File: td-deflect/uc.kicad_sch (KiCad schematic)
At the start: 20 parts, among them J4 Conn_ARM_JTAG_SWD_10, J6 Conn_01x06_Male, U12 LM1117-5.0, U2 STM32G474RETx, U23 TPS70933, U3 INA193, U4 TPS70933, X1 SG-8002CA

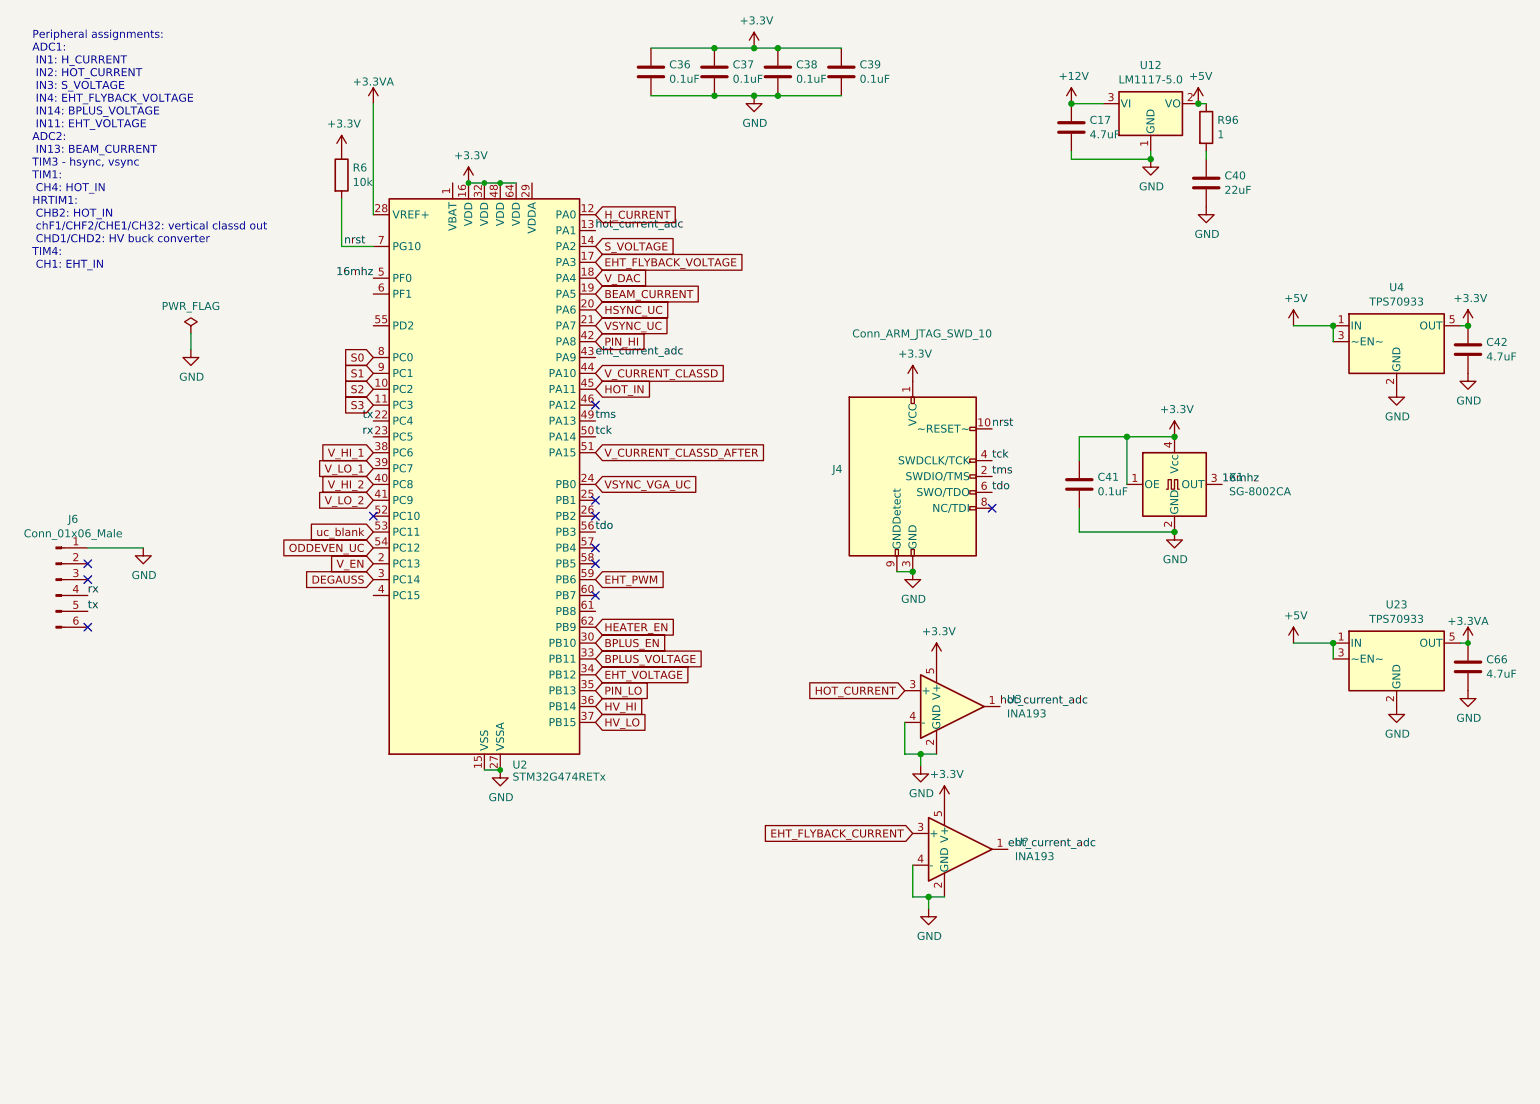
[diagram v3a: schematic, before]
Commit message: modify flyback feedback mechanism
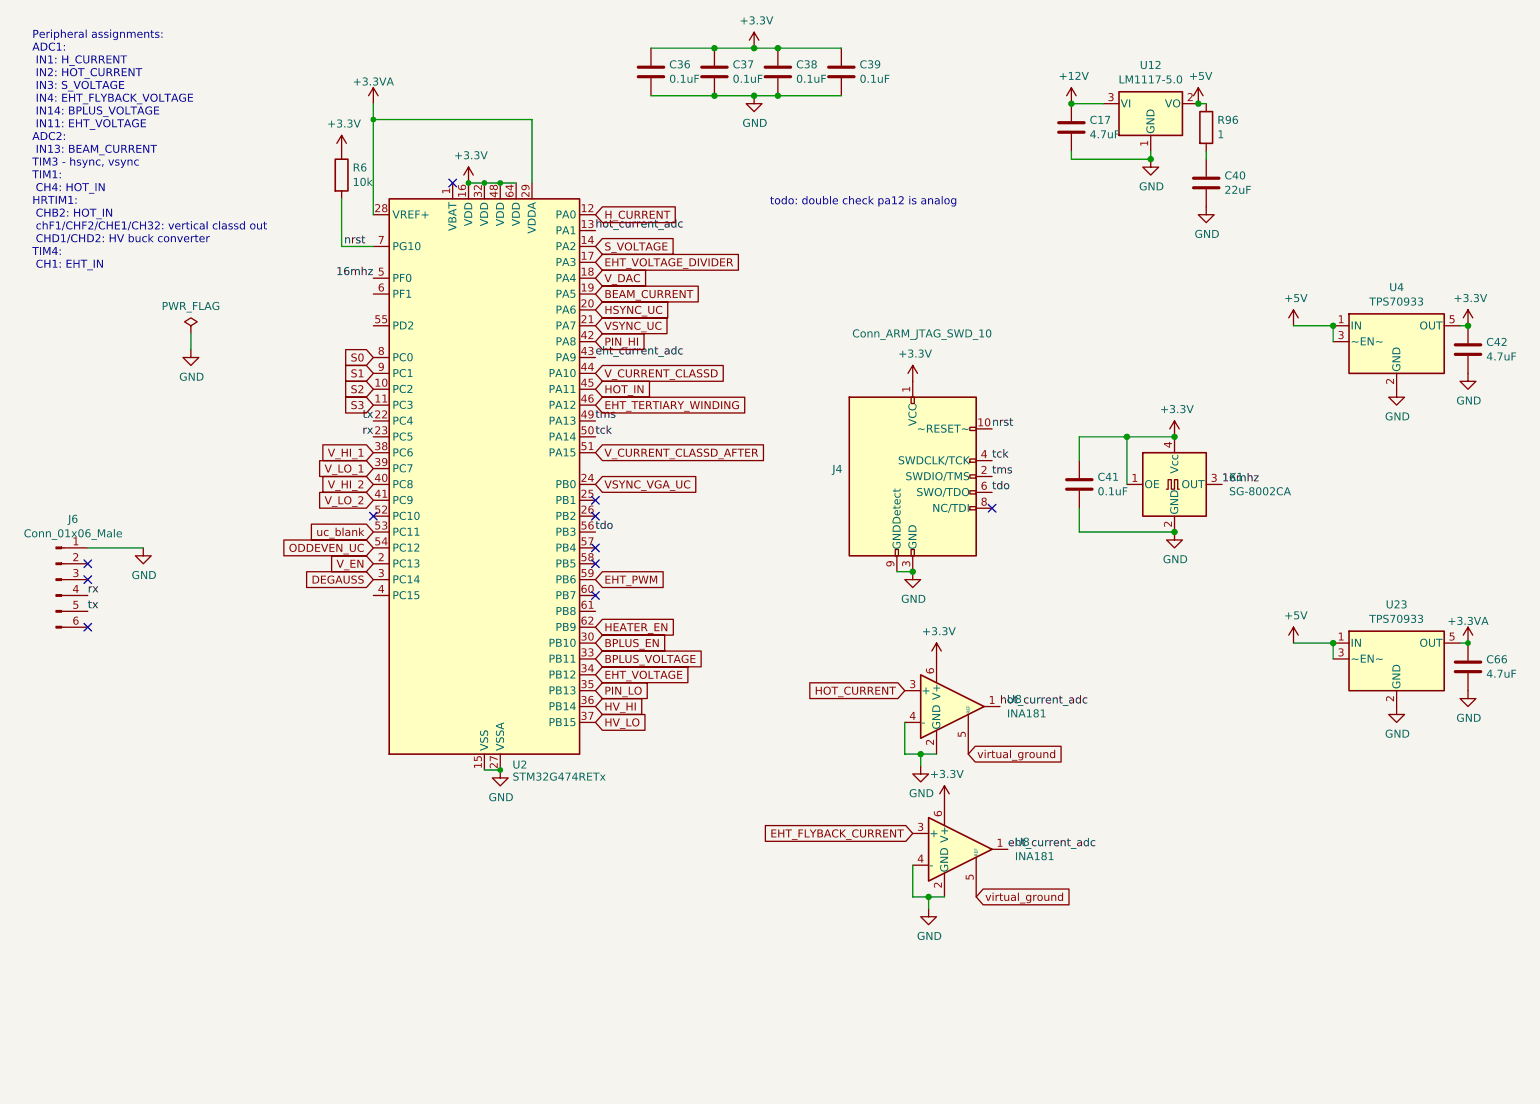
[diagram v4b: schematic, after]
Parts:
- removed U3, U?: INA193, Package_TO_SOT_SMD:SOT-23-5, symbol Amplifier_Current:INA193
- added U8 (x2): INA181, Package_TO_SOT_SMD:SOT-23-6, symbol Amplifier_Current:INA181
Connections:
- net +3.3VA: now also U2.29 (VDDA)
- net +3V3: now also U8.6 (V+), U8.6 (V+)
- net EHT_FLYBACK_CURRENT: now also U8.3 (+)
- net GND: now also U8.2 (GND), U8.2 (GND), U8.4 (-), U8.4 (-)
- net HOT_CURRENT: now also U8.3 (+)
- net eht_current_adc: now also U8.1
- net hot_current_adc: now also U8.1
- net EHT_TERTIARY_WINDING: now reaches U2.46 (PA12)
- net EHT_FLYBACK_VOLTAGE renamed EHT_VOLTAGE_DIVIDER
- new net virtual_ground: U8.5 (REF), U8.5 (REF)
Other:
- note added: "todo: double check pa12 is analog"
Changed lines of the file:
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@@
   (junction (at 224.79 83.82) (diameter 1.016) (color 0 0 0 0)
+  )
+  (junction (at 96.52 33.02) (diameter 0) (color 0 0 0 0)
   )
   (junction (at 151.13 29.21) (diameter 1.016) (color 0 0 0 0)
@@
   (no_connect (at 132.08 101.6))
   (no_connect (at 50.8 104.14))
+  (no_connect (at 109.22 43.18))
   (no_connect (at 132.08 96.52))
   (no_connect (at 50.8 114.3))
@@
   (no_connect (at 96.52 96.52))
   (no_connect (at 132.08 104.14))
-  (no_connect (at 132.08 78.74))
   (no_connect (at 132.08 93.98))
   (wire (pts (xy 208.28 39.37) (xy 220.98 39.37))
@@
     (stroke (width 0) (type solid))
   )
+  (wire (pts (xy 121.92 33.02) (xy 121.92 43.18))
+    (stroke (width 0) (type default))
+  )
   (wire (pts (xy 209.55 83.82) (xy 217.17 83.82))
     (stroke (width 0) (type solid))
@@
     (stroke (width 0) (type solid))
   )
+  (wire (pts (xy 96.52 33.02) (xy 96.52 48.26))
+    (stroke (width 0) (type default))
+  )
   (wire (pts (xy 91.44 53.34) (xy 91.44 45.72))
     (stroke (width 0) (type default))
@@
     (stroke (width 0) (type solid))
   )
+  (wire (pts (xy 96.52 33.02) (xy 121.92 33.02))
+    (stroke (width 0) (type default))
+  )
   (wire (pts (xy 182.88 157.48) (xy 185.42 157.48))
     (stroke (width 0) (type solid))
@@
     (stroke (width 0) (type default))
   )
-  (wire (pts (xy 96.52 30.48) (xy 96.52 48.26))
+  (wire (pts (xy 96.52 30.48) (xy 96.52 33.02))
     (stroke (width 0) (type default))
   )
@@
     (effects (font (size 1.27 1.27)) (justify left bottom))
   )
+  (text "todo: double check pa12 is analog" (at 160.02 46.99 0)
+    (effects (font (size 1.27 1.27)) (justify left bottom))
+  )
   (label "tx" (at 50.8 111.76 0) (fields_autoplaced)
     (effects (font (size 1.27 1.27)) (justify left bottom))
@@
   (label "rx" (at 96.52 83.82 180) (fields_autoplaced)
     (effects (font (size 1.27 1.27)) (justify right bottom))
-  )
-  (global_label "EHT_FLYBACK_VOLTAGE" (shape input) (at 132.08 55.88 0) (fields_autoplaced)
-    (effects (font (size 1.27 1.27)) (justify left))
-    (property "Intersheetrefs" "${INTERSHEET_REFS}" (at 155.7402 55.88 0)
-      (effects (font (size 1.27 1.27)) (justify left) hide)
-    )
   )
   (global_label "S0" (shape input) (at 96.52 71.12 180) (fields_autoplaced)
@@
     )
   )
+  (global_label "virtual_ground" (shape input) (at 193.04 157.48 0) (fields_autoplaced)
+    (effects (font (size 1.27 1.27)) (justify left))
+    (property "Intersheetrefs" "${INTERSHEET_REFS}" (at 208.8379 157.48 0)
+      (effects (font (size 1.27 1.27)) (justify left) hide)
+    )
+  )
   (global_label "HOT_IN" (shape input) (at 132.08 76.2 0) (fields_autoplaced)
     (effects (font (size 1.27 1.27)) (justify left))
@@
     )
   )
+  (global_label "virtual_ground" (shape input) (at 191.77 134.62 0) (fields_autoplaced)
+    (effects (font (size 1.27 1.27)) (justify left))
+    (property "Intersheetrefs" "${INTERSHEET_REFS}" (at 207.5679 134.62 0)
+      (effects (font (size 1.27 1.27)) (justify left) hide)
+    )
+  )
   (global_label "VSYNC_VGA_UC" (shape input) (at 132.08 91.44 0) (fields_autoplaced)
     (effects (font (size 1.27 1.27)) (justify left))
@@
     )
   )
+  (global_label "EHT_VOLTAGE_DIVIDER" (shape input) (at 132.08 55.88 0) (fields_autoplaced)
+    (effects (font (size 1.27 1.27)) (justify left))
+    (property "Intersheetrefs" "${INTERSHEET_REFS}" (at 154.8935 55.88 0)
+      (effects (font (size 1.27 1.27)) (justify left) hide)
+    )
+  )
   (global_label "BPLUS_VOLTAGE" (shape input) (at 132.08 119.38 0) (fields_autoplaced)
     (effects (font (size 1.27 1.27)) (justify left))
@@
     )
   )
+  (global_label "EHT_TERTIARY_WINDING" (shape input) (at 132.08 78.74 0) (fields_autoplaced)
+    (effects (font (size 1.27 1.27)) (justify left))
+    (property "Intersheetrefs" "${INTERSHEET_REFS}" (at 155.9821 78.74 0)
+      (effects (font (size 1.27 1.27)) (justify left) hide)
+    )
+  )
   (global_label "S3" (shape input) (at 96.52 78.74 180) (fields_autoplaced)
     (effects (font (size 1.27 1.27)) (justify right))
@@
         (path "/55a1a5e1-4d11-4c3e-b2b4-b9d50ddc5f9d/00000000-0000-0000-0000-00005c37bef7"
           (reference "#PWR0140") (unit 1)
-        )
-      )
-    )
-  )
-  (symbol (lib_id "Amplifier_Current:INA193") (at 189.23 127 0) (unit 1)
-    (in_bom yes) (on_board yes) (dnp no)
-    (property "Reference" "U3" (at 197.9676 125.8316 0)
-      (effects (font (size 1.27 1.27)) (justify left))
-    )
-    (property "Value" "INA193" (at 197.9676 128.143 0)
-      (effects (font (size 1.27 1.27)) (justify left))
-    )
-    (property "Footprint" "Package_TO_SOT_SMD:SOT-23-5" (at 189.23 127 0)
-      (effects (font (size 1.27 1.27)) hide)
-    )
-    (property "Datasheet" "http://www.ti.com/lit/ds/symlink/ina193.pdf" (at 189.23 127 0)
-      (effects (font (size 1.27 1.27)) hide)
-    )
-    (property "Digikey" "296-26065-1-ND" (at 189.23 127 0)
-      (effects (font (size 1.27 1.27)) hide)
-    )
-    (pin "1")
-    (pin "2")
-    (pin "3")
-    (pin "4")
-    (pin "5")
-    (instances
-      (project "td-deflect"
-        (path "/55a1a5e1-4d11-4c3e-b2b4-b9d50ddc5f9d/00000000-0000-0000-0000-00005c37bef7"
-          (reference "U3") (unit 1)
         )
       )
@@
     )
   )
-  (symbol (lib_id "Amplifier_Current:INA193") (at 190.5 149.86 0) (unit 1)
-    (in_bom yes) (on_board yes) (dnp no)
-    (property "Reference" "U?" (at 199.2376 148.6916 0)
-      (effects (font (size 1.27 1.27)) (justify left))
-    )
-    (property "Value" "INA193" (at 199.2376 151.003 0)
-      (effects (font (size 1.27 1.27)) (justify left))
-    )
-    (property "Footprint" "Package_TO_SOT_SMD:SOT-23-5" (at 190.5 149.86 0)
-      (effects (font (size 1.27 1.27)) hide)
-    )
-    (property "Datasheet" "http://www.ti.com/lit/ds/symlink/ina193.pdf" (at 190.5 149.86 0)
-      (effects (font (size 1.27 1.27)) hide)
-    )
-    (property "Digikey" "296-26065-1-ND" (at 190.5 149.86 0)
+  (symbol (lib_id "Amplifier_Current:INA181") (at 189.23 127 0) (unit 1)
+    (in_bom yes) (on_board yes) (dnp no)
+    (property "Reference" "U8" (at 197.9676 125.8316 0)
+      (effects (font (size 1.27 1.27)) (justify left))
+    )
+    (property "Value" "INA181" (at 197.9676 128.143 0)
+      (effects (font (size 1.27 1.27)) (justify left))
+    )
+    (property "Footprint" "Package_TO_SOT_SMD:SOT-23-6" (at 190.5 125.73 0)
+      (effects (font (size 1.27 1.27)) hide)
+    )
+    (property "Datasheet" "http://www.ti.com/lit/ds/symlink/ina181.pdf" (at 193.04 123.19 0)
+      (effects (font (size 1.27 1.27)) hide)
+    )
+    (property "Digikey" "296-47658-1-ND" (at 189.23 127 0)
       (effects (font (size 1.27 1.27)) hide)
     )
@@
     (pin "4")
     (pin "5")
-    (instances
-      (project "td-deflect"
-        (path "/55a1a5e1-4d11-4c3e-b2b4-b9d50ddc5f9d/00000000-0000-0000-0000-00005c37bef7"
-          (reference "U?") (unit 1)
+    (pin "6")
+    (instances
+      (project "td-deflect"
+        (path "/55a1a5e1-4d11-4c3e-b2b4-b9d50ddc5f9d"
+          (reference "U8") (unit 1)
+        )
+        (path "/55a1a5e1-4d11-4c3e-b2b4-b9d50ddc5f9d/00000000-0000-0000-0000-00005c37bef7"
+          (reference "U3") (unit 1)
         )
       )
@@
         )
       )
+    )
+  )
+  (symbol (lib_id "Amplifier_Current:INA181") (at 190.5 149.86 0) (unit 1)
+    (in_bom yes) (on_board yes) (dnp no)
+    (property "Reference" "U8" (at 199.2376 148.6916 0)
+      (effects (font (size 1.27 1.27)) (justify left))
+    )
+    (property "Value" "INA181" (at 199.2376 151.003 0)
+      (effects (font (size 1.27 1.27)) (justify left))
+    )
+    (property "Footprint" "Package_TO_SOT_SMD:SOT-23-6" (at 191.77 148.59 0)
+      (effects (font (size 1.27 1.27)) hide)
+    )
+    (property "Datasheet" "http://www.ti.com/lit/ds/symlink/ina181.pdf" (at 194.31 146.05 0)
+      (effects (font (size 1.27 1.27)) hide)
+    )
+    (property "Digikey" "296-47658-1-ND" (at 190.5 149.86 0)
+      (effects (font (size 1.27 1.27)) hide)
+    )
+    (pin "1")
+    (pin "2")
+    (pin "3")
+    (pin "4")
+    (pin "5")
+    (pin "6")
+    (instances
+      (project "td-deflect"
+        (path "/55a1a5e1-4d11-4c3e-b2b4-b9d50ddc5f9d"
+          (reference "U8") (unit 1)
+        )
+        (path "/55a1a5e1-4d11-4c3e-b2b4-b9d50ddc5f9d/00000000-0000-0000-0000-00005c37bef7"
+          (reference "U24") (unit 1)
+        )
+      )

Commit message: more updates
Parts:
- added R56, R57: R, Resistor_SMD:R_0805_2012Metric_Pad1.15x1.40mm_HandSolder, symbol Device:R
- added U25: FM24C64B, Package_SO:SOIC-8_3.9x4.9mm_P1.27mm, symbol Memory_NVRAM:FM24C64B
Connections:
- net +3V3: now also R56.1, R57.1, U25.8 (VDD)
- net EHT_TERTIARY_WINDING: now also U2.25 (PB1); no longer U2.46 (PA12)
- net GND: now also U25.1 (A0), U25.2 (A1), U25.3 (A2), U25.4 (VSS), U25.7 (WP)
- net HEATER_EN: now also U2.60 (PB7); no longer U2.62 (PB9)
- net V_CURRENT_CLASSD_AFTER: now also U2.26 (PB2); no longer U2.51 (PA15)
- net GAIN_LOAD: now reaches U2.4 (PC15)
- net SCL: now reaches U2.61 (PB8)
- net SCL: now also R57.2, U25.6 (SCL)
- new net SDA: R56.2, U2.62 (PB9), U25.5 (SDA)
- no-connect marks 11 -> 6
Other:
- note removed: "todo: double check pa12 is analog"

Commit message: small bugfix
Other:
- note added: "EN pull high to enable"
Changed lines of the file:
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@@
+    (effects (font (size 1.27 1.27)) (justify left bottom))
+  )
+  (text "EN pull high to enable" (at 247.65 83.82 0)
     (effects (font (size 1.27 1.27)) (justify left bottom))
   )

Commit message: switch to new 0805 footprint
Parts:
- C17, C36, C37, C38, C39, C41, C42, C66: footprint Capacitor_SMD:C_0805_2012Metric_Pad1.15x1.40mm_HandSolder -> Capacitor_SMD:C_0805_2012Metric_Pad1.18x1.45mm_HandSolder
- C40: footprint Capacitor_SMD:C_1206_3216Metric_Pad1.42x1.75mm_HandSolder -> Capacitor_SMD:C_1206_3216Metric_Pad1.33x1.80mm_HandSolder
- R56, R57, R6, R96: footprint Resistor_SMD:R_0805_2012Metric_Pad1.15x1.40mm_HandSolder -> Resistor_SMD:R_0805_2012Metric_Pad1.20x1.40mm_HandSolder
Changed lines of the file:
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@@
       (effects (font (size 1.27 1.27)) (justify left))
     )
-    (property "Footprint" "Capacitor_SMD:C_0805_2012Metric_Pad1.15x1.40mm_HandSolder" (at 141.9352 29.21 0)
+    (property "Footprint" "Capacitor_SMD:C_0805_2012Metric_Pad1.18x1.45mm_HandSolder" (at 141.9352 29.21 0)
       (effects (font (size 1.27 1.27)) hide)
     )
@@
       (effects (font (size 1.27 1.27)) (justify left))
     )
-    (property "Footprint" "Capacitor_SMD:C_0805_2012Metric_Pad1.15x1.40mm_HandSolder" (at 152.0952 29.21 0)
+    (property "Footprint" "Capacitor_SMD:C_0805_2012Metric_Pad1.18x1.45mm_HandSolder" (at 152.0952 29.21 0)
       (effects (font (size 1.27 1.27)) hide)
     )
@@
       (effects (font (size 1.27 1.27)) (justify left))
     )
-    (property "Footprint" "Capacitor_SMD:C_0805_2012Metric_Pad1.15x1.40mm_HandSolder" (at 162.2552 29.21 0)
+    (property "Footprint" "Capacitor_SMD:C_0805_2012Metric_Pad1.18x1.45mm_HandSolder" (at 162.2552 29.21 0)
       (effects (font (size 1.27 1.27)) hide)
     )
@@
       (effects (font (size 1.27 1.27)) (justify left))
     )
-    (property "Footprint" "Capacitor_SMD:C_0805_2012Metric_Pad1.15x1.40mm_HandSolder" (at 172.4152 29.21 0)
+    (property "Footprint" "Capacitor_SMD:C_0805_2012Metric_Pad1.18x1.45mm_HandSolder" (at 172.4152 29.21 0)
       (effects (font (size 1.27 1.27)) hide)
     )
@@
       (effects (font (size 1.27 1.27)) (justify left))
     )
-    (property "Footprint" "Capacitor_SMD:C_0805_2012Metric_Pad1.15x1.40mm_HandSolder" (at 272.7452 73.66 0)
+    (property "Footprint" "Capacitor_SMD:C_0805_2012Metric_Pad1.18x1.45mm_HandSolder" (at 272.7452 73.66 0)
       (effects (font (size 1.27 1.27)) hide)
     )
@@
       (effects (font (size 1.27 1.27)) (justify left))
     )
-    (property "Footprint" "Capacitor_SMD:C_0805_2012Metric_Pad1.15x1.40mm_HandSolder" (at 210.5152 95.25 0)
+    (property "Footprint" "Capacitor_SMD:C_0805_2012Metric_Pad1.18x1.45mm_HandSolder" (at 210.5152 95.25 0)
       (effects (font (size 1.27 1.27)) hide)
     )
@@
       (effects (font (size 1.27 1.27)) (justify left))
     )
-    (property "Footprint" "Capacitor_SMD:C_0805_2012Metric_Pad1.15x1.40mm_HandSolder" (at 209.2452 38.1 0)
+    (property "Footprint" "Capacitor_SMD:C_0805_2012Metric_Pad1.18x1.45mm_HandSolder" (at 209.2452 38.1 0)
       (effects (font (size 1.27 1.27)) hide)
     )
@@
       (effects (font (size 1.27 1.27)) (justify left))
     )
-    (property "Footprint" "Capacitor_SMD:C_1206_3216Metric_Pad1.42x1.75mm_HandSolder" (at 230.8352 46.99 0)
+    (property "Footprint" "Capacitor_SMD:C_1206_3216Metric_Pad1.33x1.80mm_HandSolder" (at 230.8352 46.99 0)
       (effects (font (size 1.27 1.27)) hide)
     )
@@
       (effects (font (size 1.27 1.27)) (justify left))
     )
-    (property "Footprint" "Resistor_SMD:R_0805_2012Metric_Pad1.15x1.40mm_HandSolder" (at 228.092 34.29 90)
+    (property "Footprint" "Resistor_SMD:R_0805_2012Metric_Pad1.20x1.40mm_HandSolder" (at 228.092 34.29 90)
       (effects (font (size 1.27 1.27)) hide)
     )
@@
       (effects (font (size 1.27 1.27)) (justify left))
     )
-    (property "Footprint" "Capacitor_SMD:C_0805_2012Metric_Pad1.15x1.40mm_HandSolder" (at 272.7452 124.46 0)
+    (property "Footprint" "Capacitor_SMD:C_0805_2012Metric_Pad1.18x1.45mm_HandSolder" (at 272.7452 124.46 0)
       (effects (font (size 1.27 1.27)) hide)
     )
@@
       (effects (font (size 1.27 1.27)) (justify left))
     )
-    (property "Footprint" "Resistor_SMD:R_0805_2012Metric_Pad1.15x1.40mm_HandSolder" (at 89.662 41.91 90)
+    (property "Footprint" "Resistor_SMD:R_0805_2012Metric_Pad1.20x1.40mm_HandSolder" (at 89.662 41.91 90)
       (effects (font (size 1.27 1.27)) hide)
     )
@@
       (effects (font (size 1.27 1.27)) (justify left))
     )
-    (property "Footprint" "Resistor_SMD:R_0805_2012Metric_Pad1.15x1.40mm_HandSolder" (at 76.962 139.7 90)
+    (property "Footprint" "Resistor_SMD:R_0805_2012Metric_Pad1.20x1.40mm_HandSolder" (at 76.962 139.7 90)
       (effects (font (size 1.27 1.27)) hide)
     )
@@
       (effects (font (size 1.27 1.27)) (justify left))
     )
-    (property "Footprint" "Resistor_SMD:R_0805_2012Metric_Pad1.15x1.40mm_HandSolder" (at 73.152 132.08 90)
-      (effects (font (size 1.27 1.27)) hide)
-    )
+    (property "Footprint" "Resistor_SMD:R_0805_2012Metric_Pad1.20x1.40mm_HandSolder" (at 73.152 132.08 90)
+      (effects (font (size 1.27 1.27)) hide)
+    )
